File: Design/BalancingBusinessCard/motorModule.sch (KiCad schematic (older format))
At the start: 2 parts

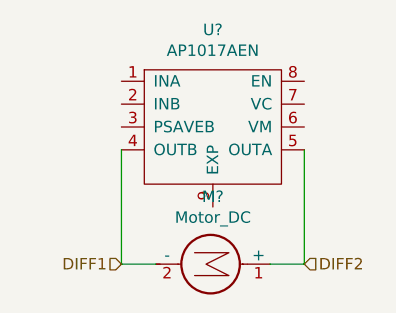
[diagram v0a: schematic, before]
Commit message: pulling ref change
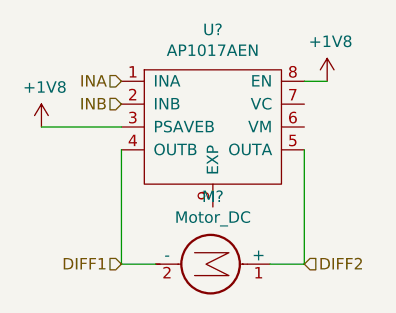
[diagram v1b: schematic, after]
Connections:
- net INA: now reaches U?.1 (INA)
- net INB: now reaches U?.2 (INB)
- net +1V8: now reaches U?.3 (PSAVEB)
- net +1V8: now also U?.8 (EN)
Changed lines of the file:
@@
 Text HLabel 4700 4400 2    50   Input ~ 0
 DIFF2
+Text HLabel 3900 3600 0    50   Input ~ 0
+INA
+Text HLabel 3900 3700 0    50   Input ~ 0
+INB
+$Comp
+L power:+1V8 #PWR?
+U 1 1 5BCBEF43
+P 4800 3600
+F 0 "#PWR?" H 4800 3450 50  0001 C CNN
+F 1 "+1V8" H 4815 3773 50  0000 C CNN
+F 2 "" H 4800 3600 50  0001 C CNN
+F 3 "" H 4800 3600 50  0001 C CNN
+	1    4800 3600
+	1    0    0    -1
+$EndComp
+$Comp
+L power:+1V8 #PWR?
+U 1 1 5BCBEF69
+P 3550 3800
+F 0 "#PWR?" H 3550 3650 50  0001 C CNN
+F 1 "+1V8" H 3565 3973 50  0000 C CNN
+F 2 "" H 3550 3800 50  0001 C CNN
+F 3 "" H 3550 3800 50  0001 C CNN
+	1    3550 3800
+	1    0    0    -1
+$EndComp
+Wire Wire Line
+	3550 3800 3900 3800
+Wire Wire Line
+	4700 3600 4800 3600
 $EndSCHEMATC
